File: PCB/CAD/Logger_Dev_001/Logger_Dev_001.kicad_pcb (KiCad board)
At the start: 2 copper layers, 54.5 x 67 mm, 74 parts, among them J1 Conn_Coaxial, J3 Micro_SD_Card_Det1, J4 Connector, USB-TYPE-C-16P, Q1 BC847BS, Q2 MMBT3904, U1 L76-M33, U2 ESP32-C6-WROOM-1, U5 AMS1117, U6 CP2102-GMR

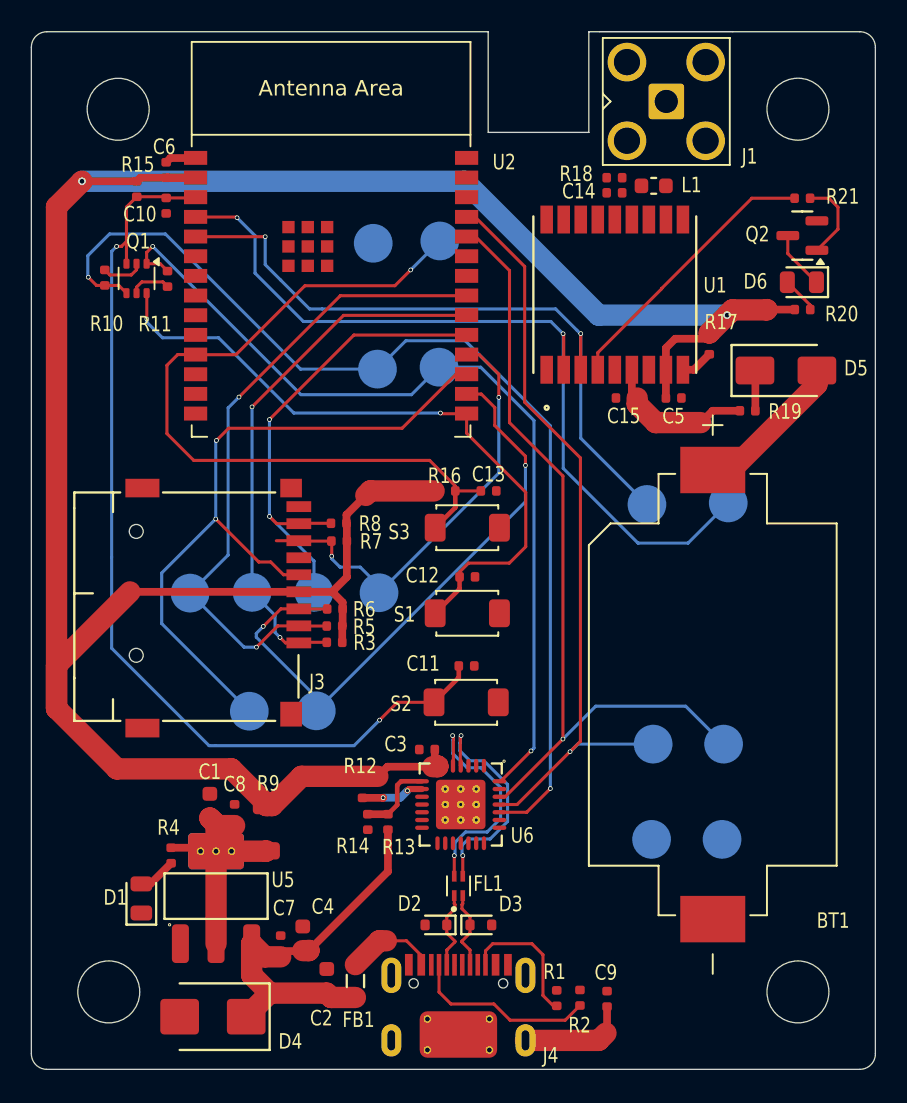
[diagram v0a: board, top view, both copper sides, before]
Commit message: PCB Board Update
GND Plane added to be improved
Need to add power plane to L1
GPS RF signal routed
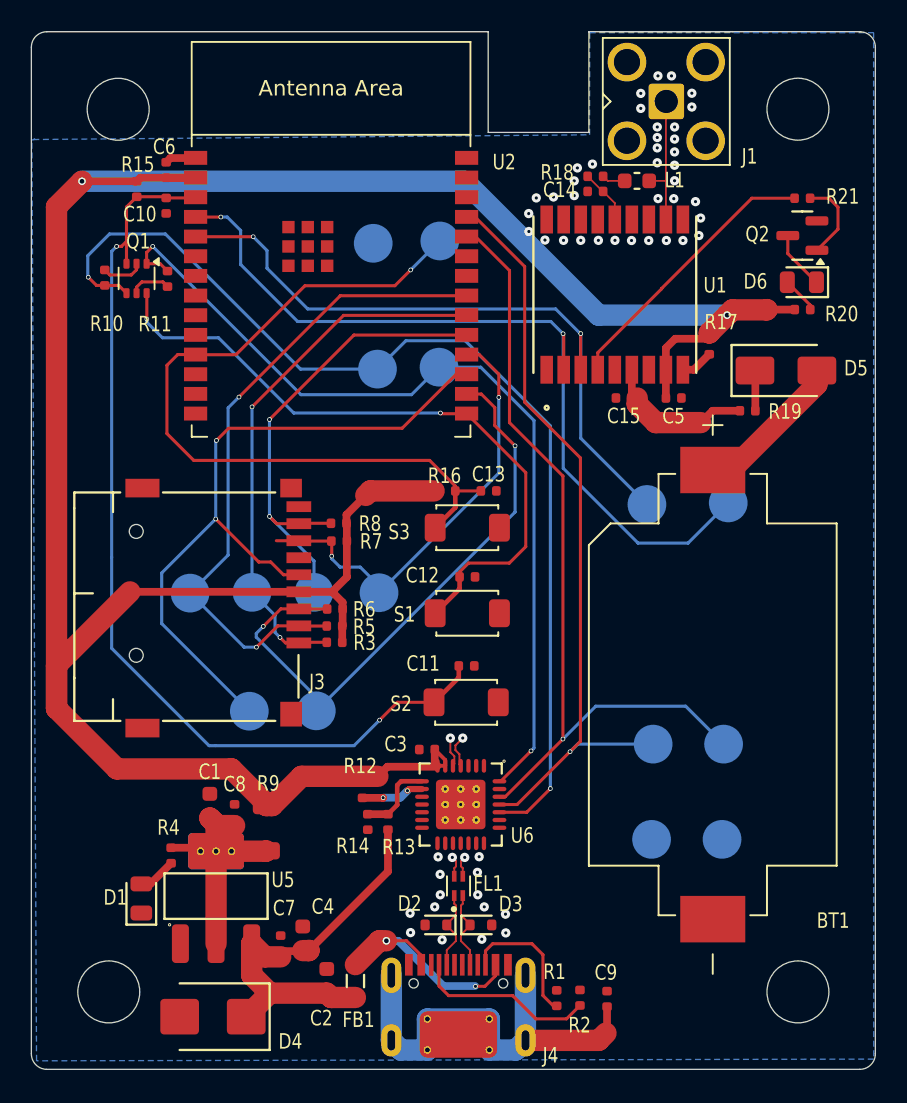
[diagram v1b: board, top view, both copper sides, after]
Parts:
- moved C14 1.23 mm to (155.2, 82.2)
- moved R18 1.23 mm to (155.2, 81.2)
- moved L1 1.13 mm to (157.9, 81.5)
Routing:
- net RF_GND: track 7.13 -> 28.7 mm
- net VUSB_UNFILTERD: track 5.86 -> 15.1 mm, vias 0 -> 2
- net Net-(J1-In): track 0.00 -> 8.72 mm
- net Net-(U1-VCC_REF): track 0.00 -> 3.53 mm
- net Net-(L1-Pad1): track 0.00 -> 1.52 mm
- net 3v3_VCC: track 169.5 -> 170.5 mm
- net /USB C COMs 3v3 Power Input Module/USB_D+: track 15.0 -> 13.9 mm
- net /USB C COMs 3v3 Power Input Module/USB_D-: track 15.0 -> 13.9 mm
- net /SDIO_CMD: track 40.0 -> 39.5 mm
- net GND: vias 0 -> 66
- added copper zone on B.Cu, net GND
- added copper zone on In1.Cu, net GND
- added copper zone on In2.Cu, net GND
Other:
- copper layers 2 -> 4

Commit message: BCB Board Update
Planes poured and general wiring completed. All vias updated. 3D models completed.

To check:
- footprints
- rules
-BOM cost
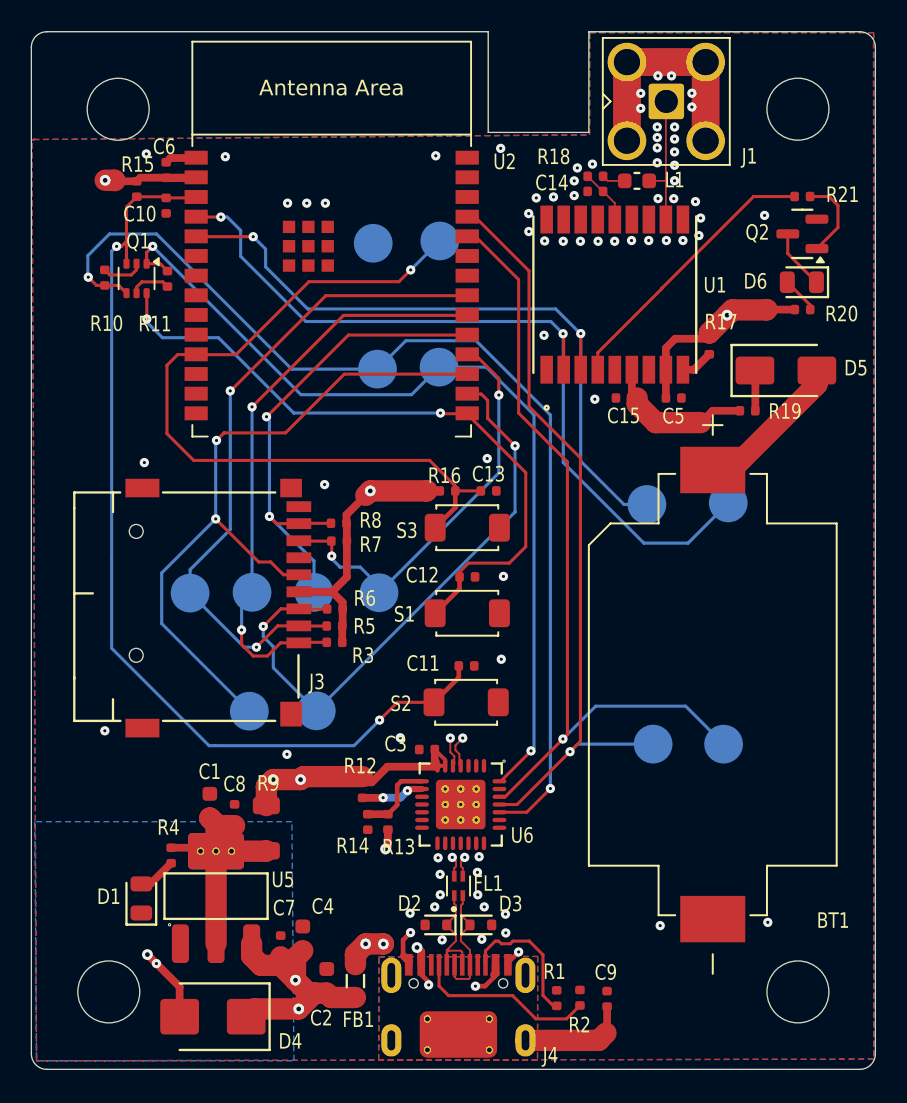
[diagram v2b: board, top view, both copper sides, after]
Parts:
- removed TP5: USB_D+_TP, TestPoint:TestPoint_Pad_D2.5mm
- removed TP6: USB_D-_TP, TestPoint:TestPoint_Pad_D2.5mm
- moved U2 13.3 mm to (129.2, 98.1)
- moved Q2 0.11 mm to (168.6, 85.0)
- moved R21 0.11 mm to (168.6, 82.5)
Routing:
- net 3v3_VCC: track 170.5 -> 54.0 mm, vias 2 -> 5
- net GND: track 2.01 -> 25.7 mm, vias 66 -> 89
- net RF_GND: track 28.7 -> 7.13 mm
- net VUSB: track 25.5 -> 17.6 mm, vias 0 -> 3
- net VUSB_UNFILTERD: track 15.1 -> 7.78 mm, vias 2 -> 5
- net /SDIO_DATA2: track 35.1 -> 38.1 mm
- net /USB C COMs 3v3 Power Input Module/USB_UNF_D+: track 5.29 -> 7.99 mm
- net /USB C COMs 3v3 Power Input Module/USB_UNF_D-: track 5.28 -> 7.94 mm
- net /SDIO_DATA0: track 28.9 -> 27.2 mm
- net /GPS_RX: track 43.3 -> 44.1 mm
- net /SDIO_DATA3: track 42.2 -> 42.8 mm
- net /GPS_TX: track 52.9 -> 52.4 mm
- net /SDIO_CMD: track 39.5 -> 40.0 mm
- added copper zone on In2.Cu, net 3v3_VCC
- added copper zone on F.Cu, net GND
- added copper zone on B.Cu, net Net-(C1-Pad1)
- added copper zone on In2.Cu, net Net-(C1-Pad1)
- added copper zone on B.Cu, net RF_GND
- added copper zone on F.Cu, net RF_GND
- added copper zone on In2.Cu, net VUSB
- added copper zone on In2.Cu, net VUSB_UNFILTERD

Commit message: PCB_Board Update
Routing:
- net GND: track 25.7 -> 27.6 mm, vias 89 -> 92

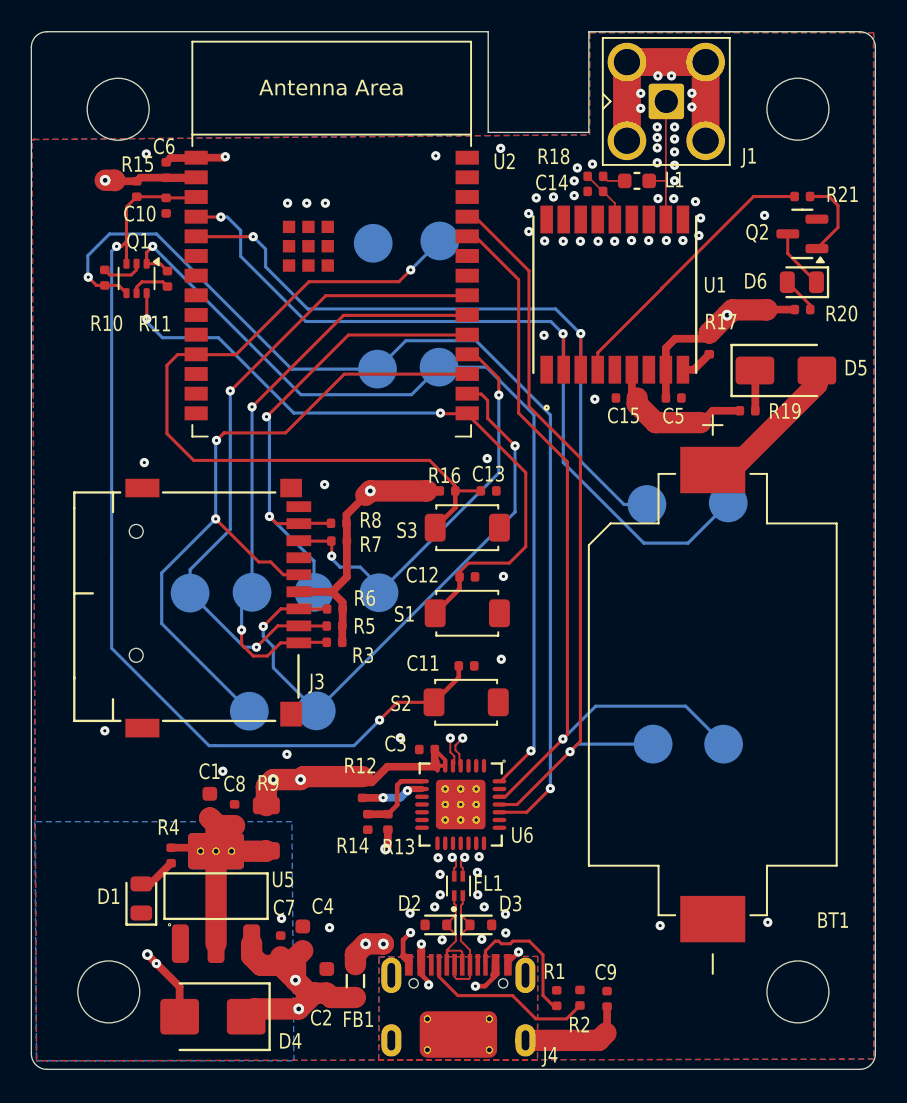
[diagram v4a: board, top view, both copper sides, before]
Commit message: Update via size to reduce cost
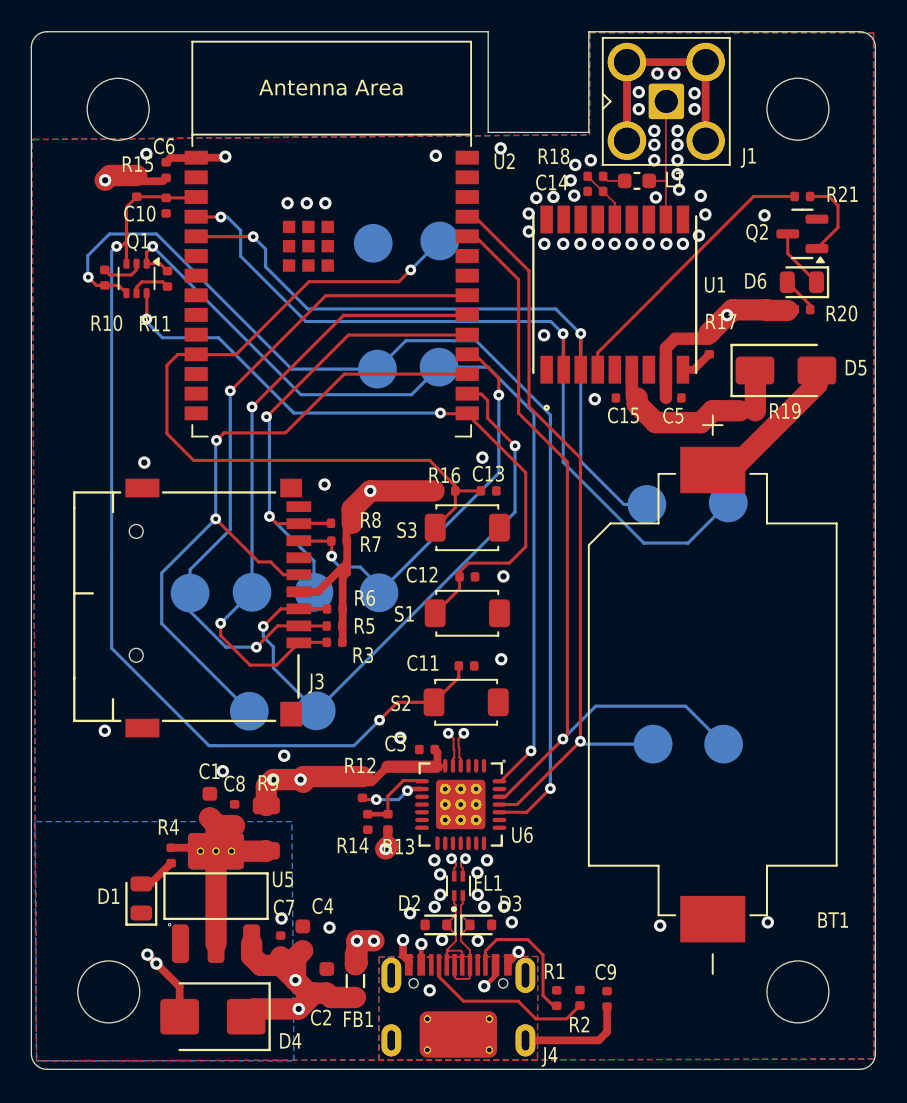
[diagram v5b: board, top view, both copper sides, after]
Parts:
- FB1: value ~ -> 100Ω@100MHz 150mΩ 800mA
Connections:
- C9 pad 1: RF_GND -> GND
- J4 pad S1: RF_GND -> GND
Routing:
- net RF_GND: track 7.13 -> 0.00 mm
- net GND: track 27.6 -> 34.0 mm, vias 92 -> 90
- net 3v3_VCC: track 54.0 -> 49.9 mm
- net Net-(D5-Pad1): track 2.61 -> 0.00 mm
- net VBAT_2032: track 9.67 -> 12.2 mm
- net /SDIO_DATA2: track 38.1 -> 40.2 mm
- net VUSB_UNFILTERD: track 7.89 -> 6.42 mm
- net /USBC_RX: track 49.7 -> 48.9 mm
- net /USB C COMs 3v3 Power Input Module/USB_D+: track 13.9 -> 14.6 mm
- net /USB C COMs 3v3 Power Input Module/USB_D-: track 13.9 -> 14.6 mm
- net /SDIO_DATA3: track 42.8 -> 43.5 mm
- removed copper zone on B.Cu, net RF_GND
- removed copper zone on F.Cu, net RF_GND

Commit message: Dielectric change to make cheaper
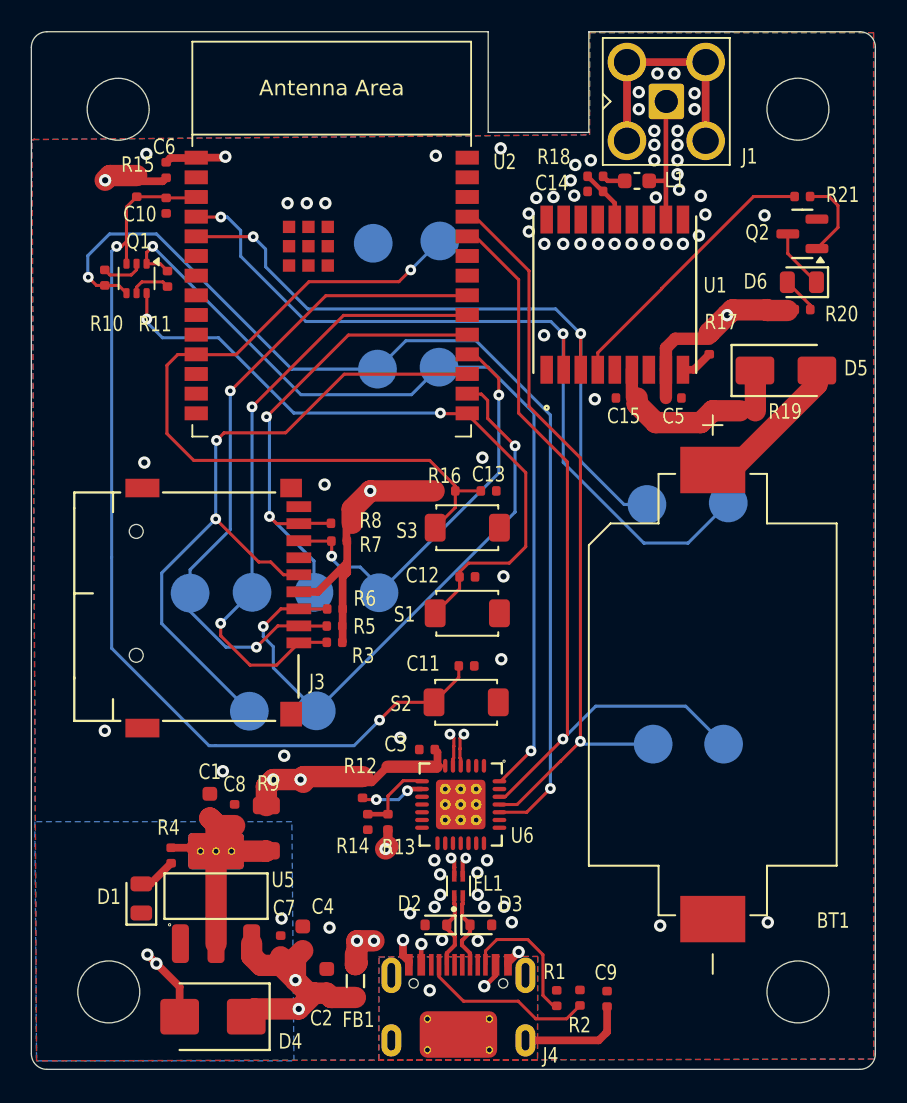
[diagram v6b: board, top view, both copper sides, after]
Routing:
- net /USB C COMs 3v3 Power Input Module/USB_UNF_D+: track 7.99 -> 5.13 mm
- net /USB C COMs 3v3 Power Input Module/USB_UNF_D-: track 7.94 -> 5.13 mm
